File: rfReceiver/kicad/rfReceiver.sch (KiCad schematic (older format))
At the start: 13 parts, among them J1 MAX485AB, J2 RF module, J3 POWER, Q1 BC547, U1 MAX485E

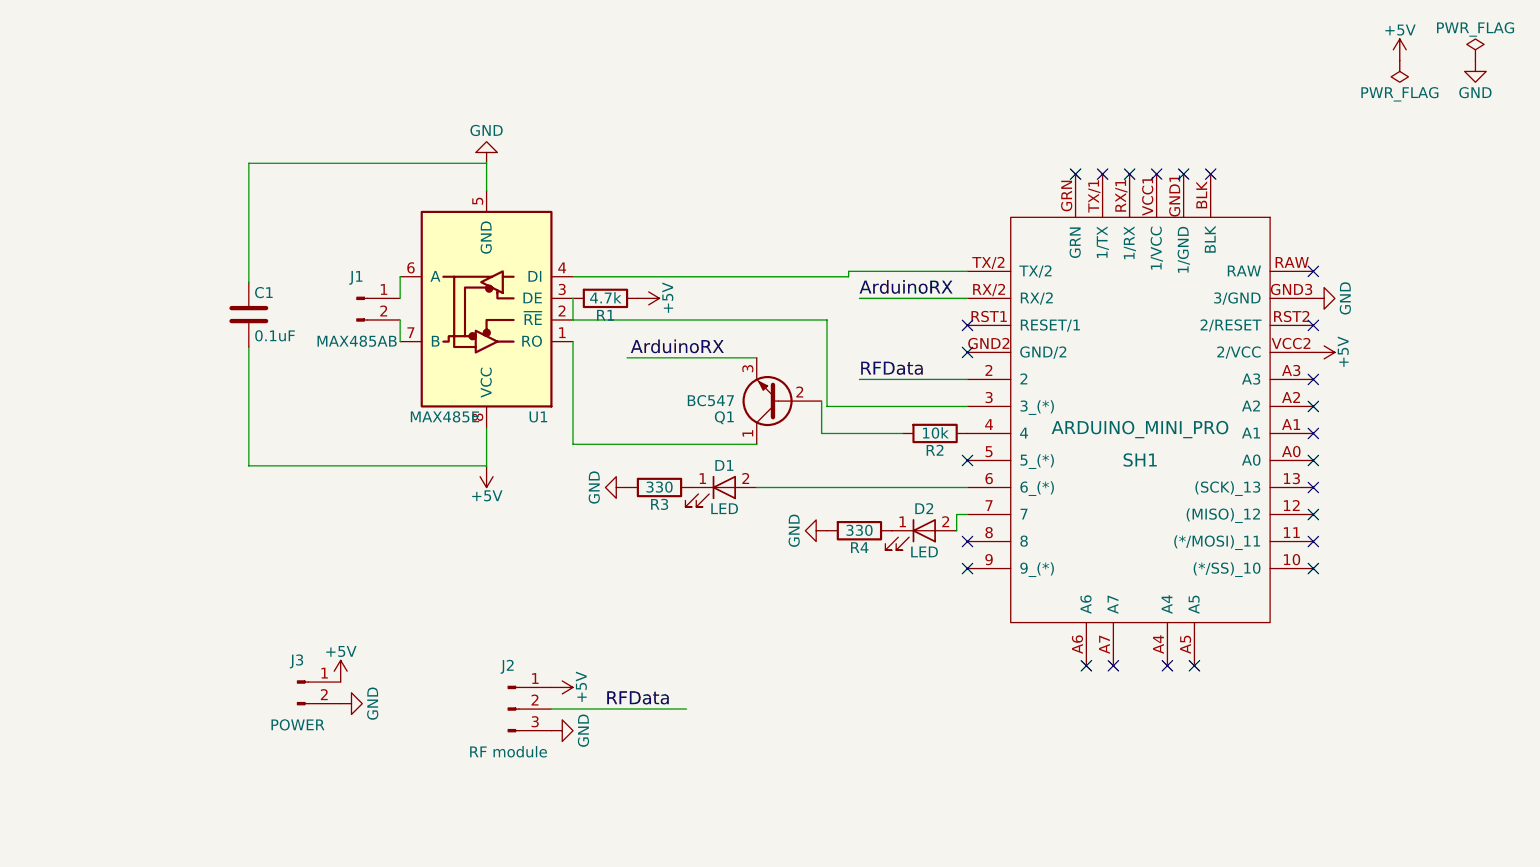
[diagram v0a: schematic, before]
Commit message: update kicad schema
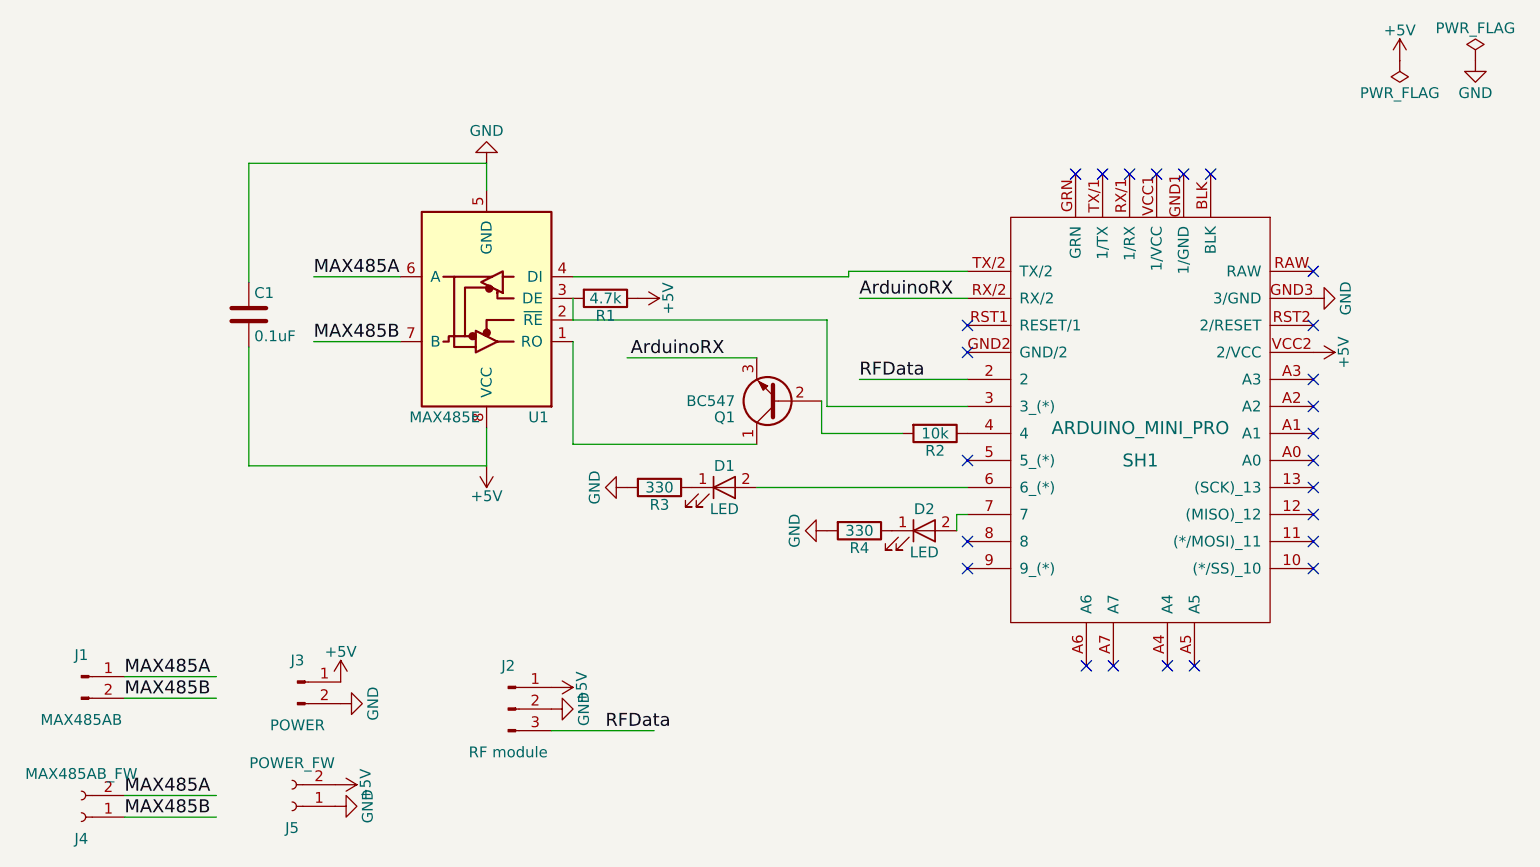
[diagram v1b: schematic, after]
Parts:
- added J4: MAX485AB_FW, Socket_Strips:Socket_Strip_Straight_1x02_Pitch2.54mm, symbol Conn_01x02_Female
- added J5: POWER_FW, Socket_Strips:Socket_Strip_Straight_1x02_Pitch2.54mm, symbol Conn_01x02_Female
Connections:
- net labels added: MAX485A, MAX485B
- wire segments 26 -> 30
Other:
- moved on the sheet: J1
